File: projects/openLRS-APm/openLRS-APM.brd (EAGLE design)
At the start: 43.1 x 20.7 mm, 26 parts, among them IC2 RFM23BPSMD, J1 AVR_SPI_PRG_6PTH, U1 ATMEGA328P, Y1 16MHz

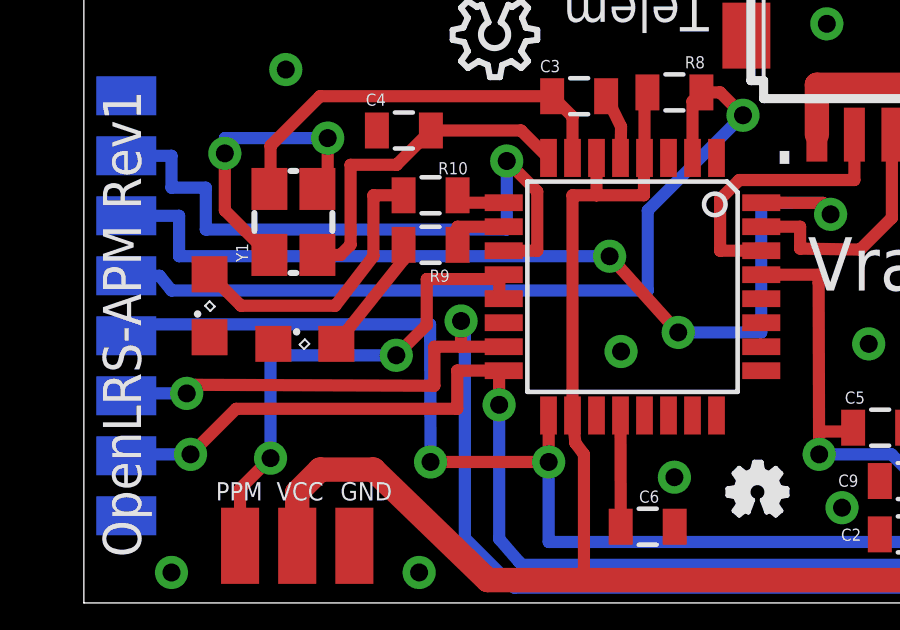
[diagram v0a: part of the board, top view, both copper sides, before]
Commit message: Revert 0493923..5027763
This rolls back to commit 049392304cea7ab2cd1e886349edb191a1876f4a.
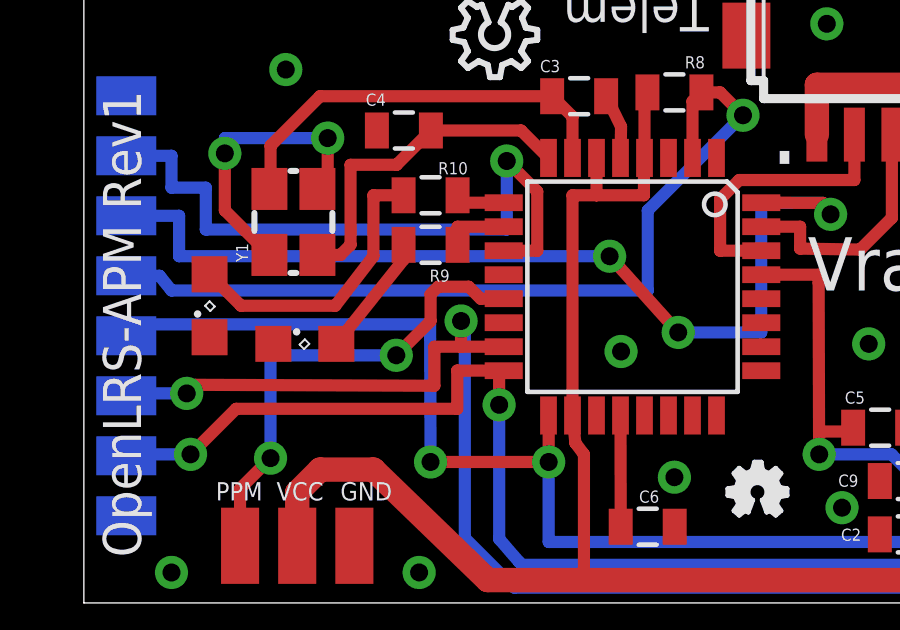
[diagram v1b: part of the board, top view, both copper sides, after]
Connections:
- net PPM: no longer U1.12
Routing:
- net PPM: track 17.3 -> 16.2 mm
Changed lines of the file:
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@@
 <wire x1="5.207" y1="3.81" x2="5.207" y2="1.905" width="0.4064" layer="1"/>
 <contactref element="U1" pad="13"/>
-<wire x1="10.414" y1="8.255" x2="11.43" y2="9.271" width="0.4064" layer="1"/>
-<contactref element="U1" pad="12"/>
-<wire x1="11.43" y1="9.271" x2="11.43" y2="10.795" width="0.4064" layer="1"/>
-<wire x1="11.43" y1="10.795" x2="13.8494" y2="10.795" width="0.4064" layer="1"/>
-<wire x1="13.8494" y1="10.795" x2="13.9954" y2="10.941" width="0.4064" layer="1"/>
-<wire x1="13.8494" y1="10.795" x2="13.8494" y2="10.287" width="0.4064" layer="1"/>
-<wire x1="13.8494" y1="10.287" x2="13.9954" y2="10.141" width="0.4064" layer="1"/>
+<wire x1="10.414" y1="8.255" x2="11.557" y2="9.398" width="0.4064" layer="1"/>
+<wire x1="11.557" y1="9.398" x2="11.557" y2="10.287" width="0.4064" layer="1"/>
+<wire x1="13.9954" y1="10.141" x2="13.227" y2="10.141" width="0.4064" layer="1"/>
+<wire x1="13.227" y1="10.141" x2="12.827" y2="10.541" width="0.4064" layer="1"/>
+<wire x1="12.827" y1="10.541" x2="11.811" y2="10.541" width="0.4064" layer="1"/>
+<wire x1="11.811" y1="10.541" x2="11.557" y2="10.287" width="0.4064" layer="1"/>
 </signal>
 </signals>
